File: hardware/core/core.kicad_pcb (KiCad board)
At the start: 2 copper layers, 228.6 x 129.5 mm, 102 parts, among them J1 9V_IN, J2 MIDI IN, J3 MIDI OUT 1, J4 SWITCHES OUT, J5 EXP/AUX IN, J7 LCD, J8 USB_C_Receptacle_USB2.0_16P, J9 MIDI OUT 2/3, K1 G5V-1, K2 G5V-1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

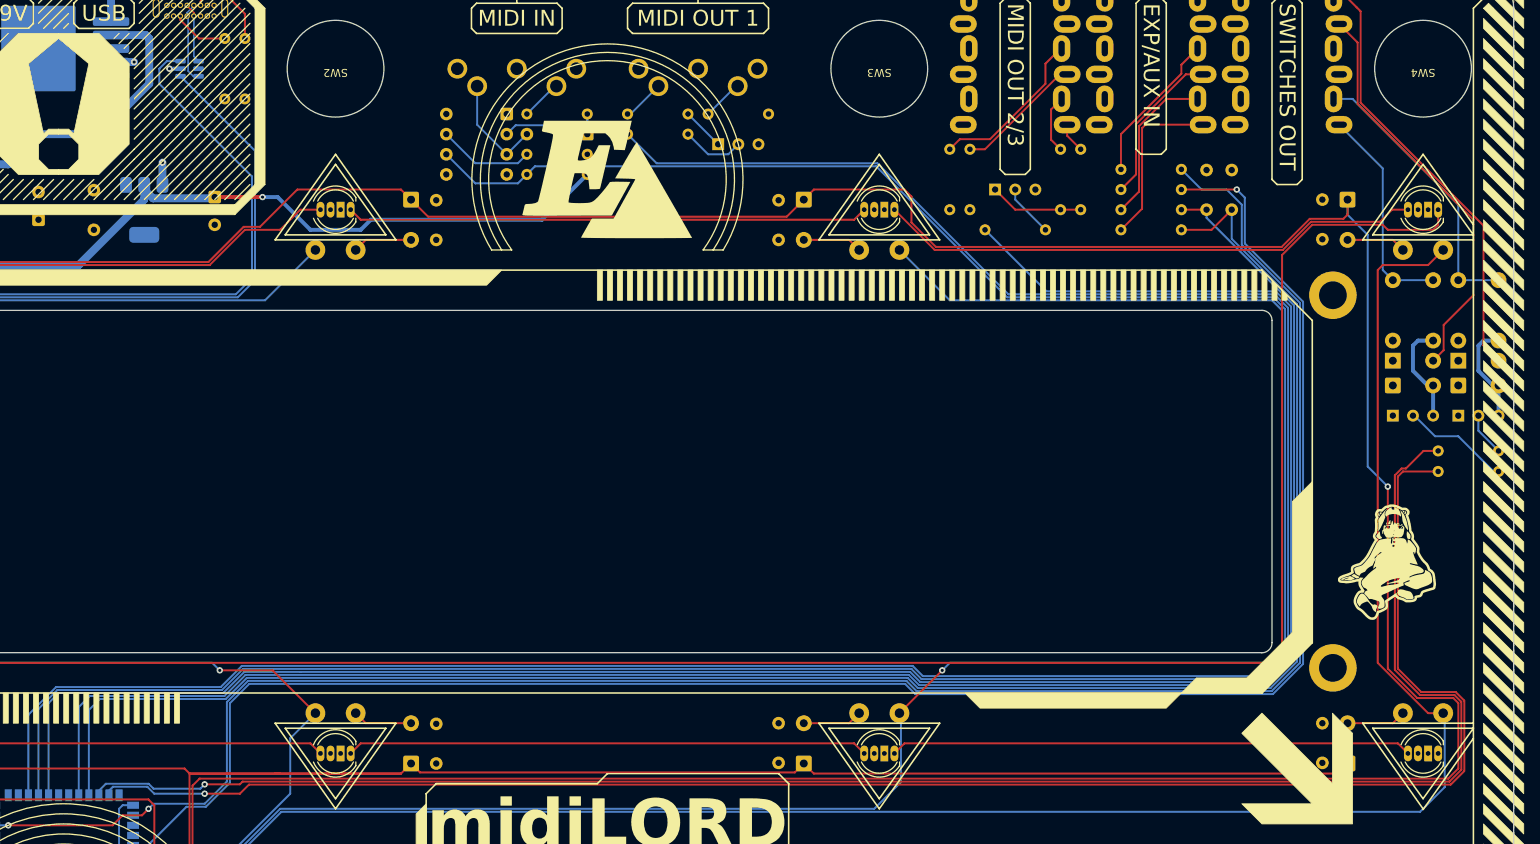
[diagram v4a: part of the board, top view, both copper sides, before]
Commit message: Update PCB layout with revised nets and add D21 WS2812B LED
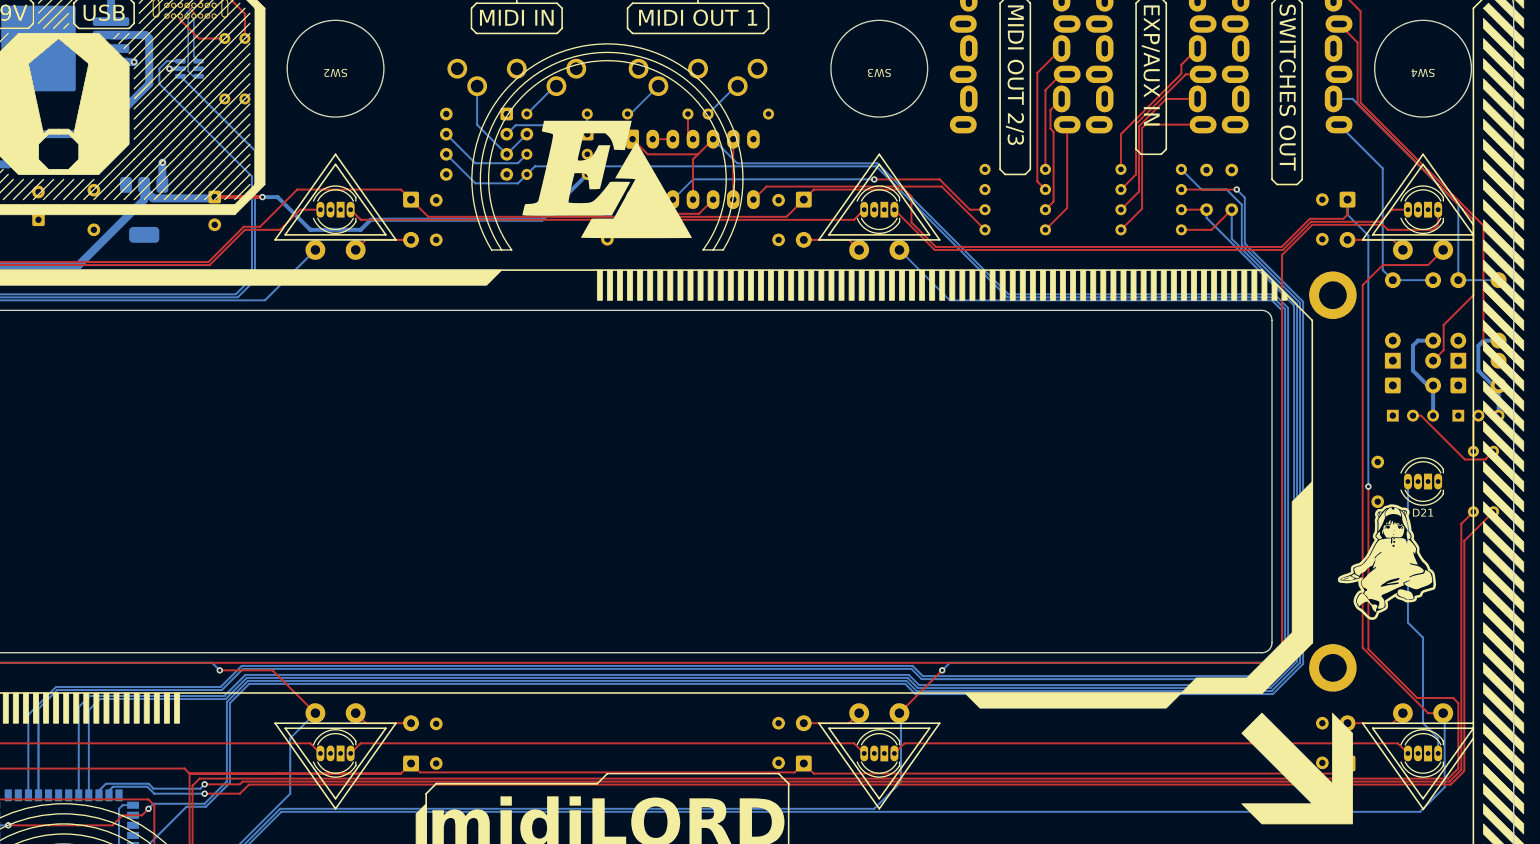
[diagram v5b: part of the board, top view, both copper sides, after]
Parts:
- removed Q1, Q2: 2N3906, Package_TO_SOT_THT:TO-92_Inline_Wide
- removed R17, R18: 4.7K, Resistor_THT:R_Axial_DIN0204_L3.6mm_D1.6mm_P7.62mm_Horizontal
- added C18: 100n, Capacitor_THT:C_Rect_L7.0mm_W2.5mm_P5.00mm, B.Cu at (300.4, 149.9)
- added C19: 100n, Capacitor_THT:C_Rect_L7.0mm_W2.5mm_P5.00mm, B.Cu at (203.2, 116.8)
- added D21: WS2812B, midilord:APA106, F.Cu at (306.1, 152.4)
- added U6: 74HC04, Package_DIP:DIP-14_W7.62mm_Socket_LongPads, B.Cu at (206.4, 109.2)
- moved R7 13.1 mm to (258.4, 115.6), turned to 180 degrees
- moved R8 12.3 mm to (250.8, 120.7), turned to 0 degrees
- moved R6 9.53 mm to (250.8, 118.1), turned to 0 degrees
- moved R9 8.87 mm to (312.4, 156.2), turned to 90 degrees
- moved R10 8.64 mm to (315.0, 156.2), turned to 90 degrees
- moved R5 5.43 mm to (250.8, 113.0), turned to 0 degrees
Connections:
- D10 pad 2: unconnected-(D10-DOUT-Pad2) -> Net-(D10-DOUT)
- R6 pad 1: Net-(Q2-E) -> Net-(R6-Pad1)
- R8 pad 1: Net-(Q2-E) -> Net-(R8-Pad1)
- U3 pad 18: MIDI_OUT1 -> MIDI_OUT
- U3 pad 19: MIDI_OUT2 -> unconnected-(U3-IO11-Pad19)
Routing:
- net MIDI_OUT: track 0.00 -> 315.4 mm
- net MIDI_OUT1: track 308.7 -> 0.00 mm
- net MIDI_OUT2: track 258.8 -> 0.00 mm
- net Net-(R6-Pad1): track 0.00 -> 42.0 mm, vias 0 -> 1
- net Net-(D10-DOUT): track 0.00 -> 35.9 mm
- net Net-(R8-Pad1): track 0.00 -> 32.2 mm
- net SW_OUT1: track 223.9 -> 207.2 mm
- net SW_OUT2: track 221.8 -> 207.5 mm
- net Net-(Q2-E): track 11.8 -> 0.00 mm
- net Net-(J9-2T): track 3.81 -> 14.4 mm
- net Net-(U6-Pad10): track 0.00 -> 9.10 mm
- net Net-(Q1-B): track 7.93 -> 0.00 mm
- net Net-(J9-T): track 7.39 -> 15.1 mm
- net Net-(U6-Pad6): track 0.00 -> 7.62 mm
- net Net-(Q2-B): track 6.66 -> 0.00 mm
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
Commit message: Update PCB layout and fix DRC warnings for unconnected pins
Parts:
- U6: value 74HC04 -> 74HCT04
- moved G*** 51.3 mm to (271.8, 203.8)
